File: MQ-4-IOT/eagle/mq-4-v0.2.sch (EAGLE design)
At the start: 3 parts

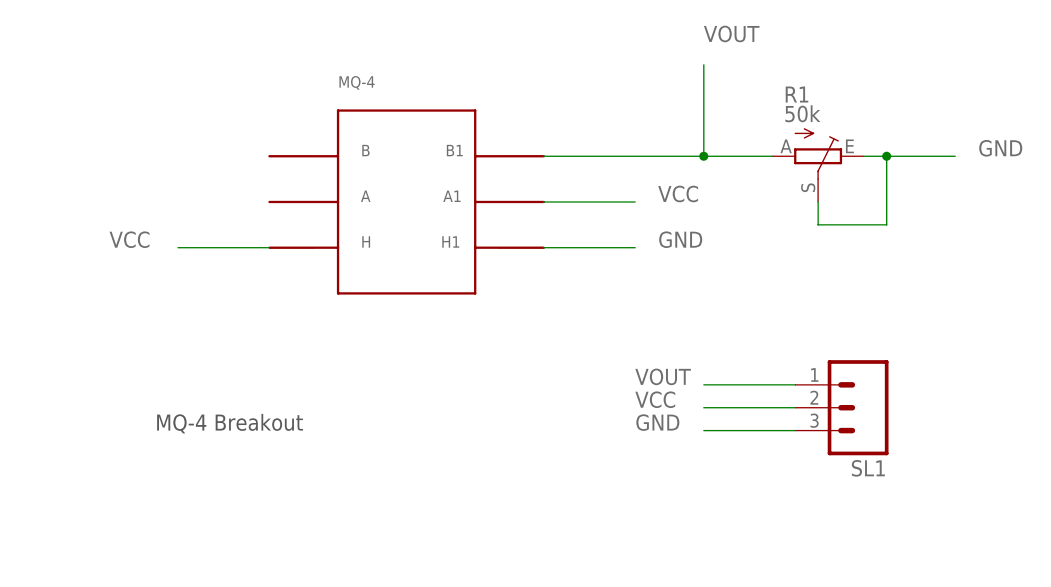
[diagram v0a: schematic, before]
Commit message: Added enclosure top half.
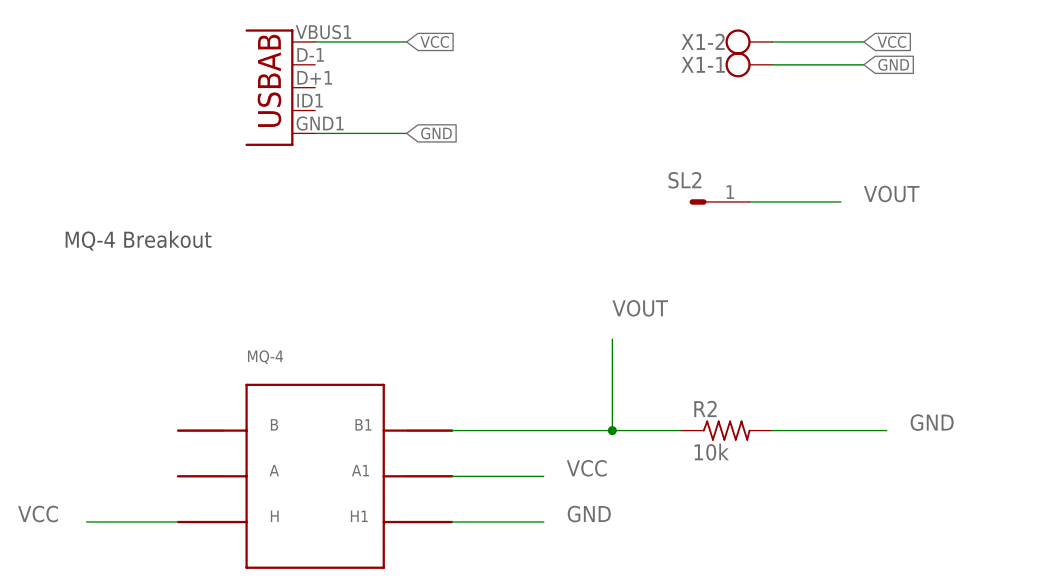
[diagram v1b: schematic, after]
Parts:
- removed R1: 50k, pot:TRIM_EU-B64Y
- removed SL1: (no value), con-amp-quick:M03
- added R2: 10k, rcl:R-US_M0805
- added SL2: (no value), pads:M0201P
- added U$4: (no value), Testing:USB-AB""
- added X1: (no value), con-wago-500:W237-102
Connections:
- net GND: now also R2.2, U$4.GND, X1-1.KL; no longer R1.E, R1.S, SL1.3
- net VCC: now also U$4.VBUS, X1-2.KL; no longer SL1.2
- net VOUT: now also R2.1, SL2.1; no longer R1.A, SL1.1

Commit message: Added CAM files.
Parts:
- removed R2: 10k, rcl:R-US_M0805
- removed U$4: (no value), Testing:USB-AB""
- added R4: 10k, rcl:R-US_0207/10
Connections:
- net GND: now also R4.1, X1-2.KL; no longer R2.2, U$4.GND, X1-1.KL
- net VCC: now also X1-1.KL; no longer U$4.VBUS, X1-2.KL
- net VOUT: now also R4.2; no longer R2.1
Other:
- moved on the sheet: SL2
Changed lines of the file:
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@@
 </variantdefs>
 <classes>
-<class number="0" name="default" width="0.1524" drill="0">
-<clearance class="0" value="0.1524"/>
+<class number="0" name="default" width="0.9144" drill="0.254">
+<clearance class="0" value="0.508"/>
 </class>
-<class number="1" name="Power" width="0.4064" drill="0.6096">
-<clearance class="1" value="0.1524"/>
+<class number="1" name="GND" width="0.9144" drill="0.254">
+<clearance class="1" value="0.508"/>
 </class>
 </classes>
 <parts>
 <part name="U$1" library="mq-x" deviceset="MQ-4" device=""/>
-<part name="U$4" library="Testing" deviceset="USB-AB" device="&quot;&quot;"/>
 <part name="X1" library="con-wago-500" deviceset="W237-102" device=""/>
 <part name="SL2" library="pads" deviceset="M02" device="01P"/>
-<part name="R2" library="rcl" deviceset="R-US_" device="M0805" value="10k"/>
+<part name="R4" library="rcl" deviceset="R-US_" device="0207/10" value="10k"/>
 </parts>
 <sheets>
@@
 <instances>
 <instance part="U$1" gate="G$1" x="43.18" y="15.24"/>
-<instance part="U$4" gate="G$1" x="38.1" y="58.42" rot="R180"/>
 <instance part="X1" gate="-1" x="88.9" y="60.96"/>
 <instance part="X1" gate="-2" x="88.9" y="63.5"/>
-<instance part="SL2" gate="G$1" x="83.82" y="45.72"/>
-<instance part="R2" gate="G$1" x="88.9" y="20.32"/>
+<instance part="SL2" gate="G$1" x="35.56" y="60.96"/>
+<instance part="R4" gate="G$1" x="88.9" y="20.32" smashed="yes" rot="R180">
+<attribute name="NAME" x="85.598" y="24.3586" size="1.778" layer="95"/>
+<attribute name="VALUE" x="86.868" y="14.478" size="1.778" layer="96"/>
+</instance>
 </instances>
 <busses>
@@
 </segment>
 <segment>
-<pinref part="X1" gate="-2" pin="KL"/>
-<wire x1="93.98" y1="63.5" x2="104.14" y2="63.5" width="0.1524" layer="91"/>
-</segment>
-<segment>
-<pinref part="U$4" gate="G$1" pin="VBUS"/>
-<wire x1="43.18" y1="63.5" x2="53.34" y2="63.5" width="0.1524" layer="91"/>
-<label x="53.34" y="63.5" size="1.27" layer="95" xref="yes"/>
-<label x="104.14" y="63.5" size="1.27" layer="95" xref="yes"/>
+<pinref part="X1" gate="-1" pin="KL"/>
+<wire x1="93.98" y1="60.96" x2="104.14" y2="60.96" width="0.1524" layer="91"/>
 </segment>
 </net>
@@
 </segment>
 <segment>
-<pinref part="U$4" gate="G$1" pin="GND"/>
-<wire x1="43.18" y1="53.34" x2="53.34" y2="53.34" width="0.1524" layer="91"/>
-<label x="53.34" y="53.34" size="1.27" layer="95" xref="yes"/>
-<label x="104.14" y="60.96" size="1.27" layer="95" xref="yes"/>
+<wire x1="93.98" y1="20.32" x2="106.68" y2="20.32" width="0.1524" layer="91"/>
+<label x="109.22" y="20.32" size="1.778" layer="95"/>
+<pinref part="R4" gate="G$1" pin="1"/>
 </segment>
 <segment>
-<pinref part="X1" gate="-1" pin="KL"/>
-<wire x1="93.98" y1="60.96" x2="104.14" y2="60.96" width="0.1524" layer="91"/>
-</segment>
-<segment>
-<wire x1="93.98" y1="20.32" x2="106.68" y2="20.32" width="0.1524" layer="91"/>
-<label x="109.22" y="20.32" size="1.778" layer="95"/>
-<pinref part="R2" gate="G$1" pin="2"/>
+<pinref part="X1" gate="-2" pin="KL"/>
+<wire x1="93.98" y1="63.5" x2="104.14" y2="63.5" width="0.1524" layer="91"/>
 </segment>
 </net>
@@
 <junction x="76.2" y="20.32"/>
 <label x="76.2" y="33.02" size="1.778" layer="95"/>
-<pinref part="R2" gate="G$1" pin="1"/>
+<pinref part="R4" gate="G$1" pin="2"/>
 </segment>
 <segment>
 <pinref part="SL2" gate="G$1" pin="1"/>
-<wire x1="91.44" y1="45.72" x2="101.6" y2="45.72" width="0.1524" layer="91"/>
-<label x="104.14" y="45.72" size="1.778" layer="95"/>
+<wire x1="43.18" y1="60.96" x2="53.34" y2="60.96" width="0.1524" layer="91"/>
+<label x="55.88" y="60.96" size="1.778" layer="95"/>
 </segment>
 </net>
